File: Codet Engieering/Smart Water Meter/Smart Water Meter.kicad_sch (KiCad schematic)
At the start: 30 parts, among them J1 Barrel_Jack_Switch, J3 Conn_01x12_Pin, J4 Conn_01x07_Pin, J5 Conn_01x08_Pin, J6 Screw_Terminal_01x02, J6 Screw_Terminal_01x03, K2 SRD-05VDC-SL-C, Q2 BC547, U3 L7805CV

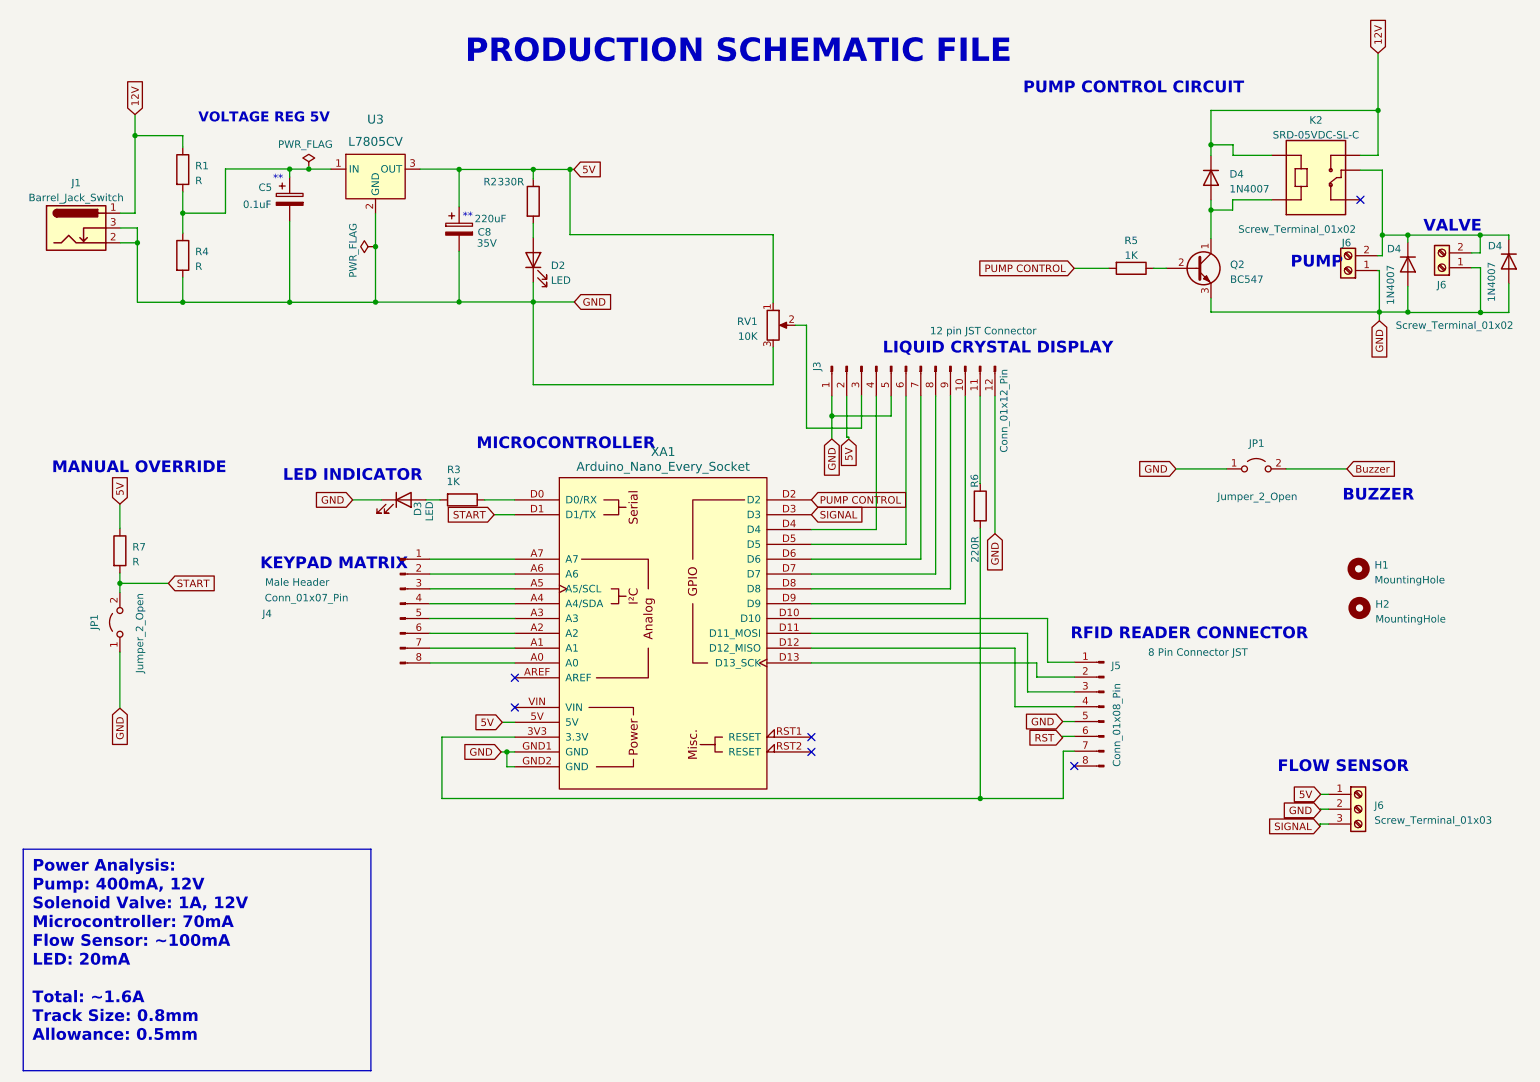
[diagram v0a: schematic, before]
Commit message: Redessigned the board to fit into asingle layer pcb for local production
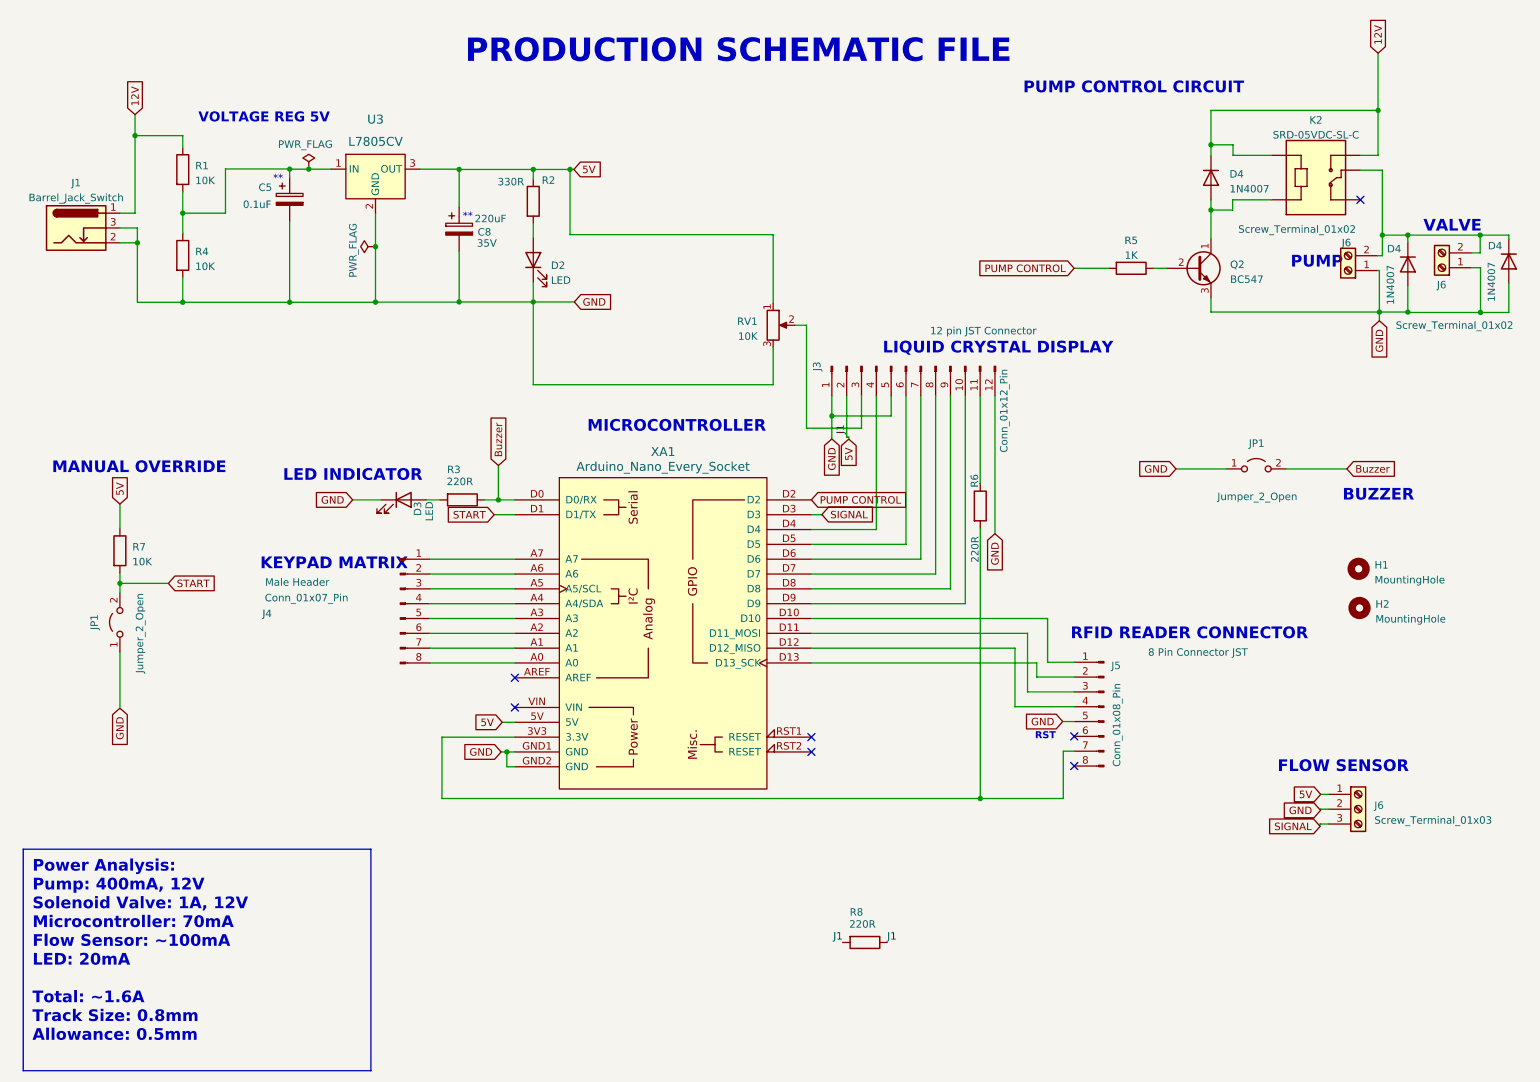
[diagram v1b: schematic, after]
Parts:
- added R8: 220R, Resistor_THT:R_Axial_DIN0207_L6.3mm_D2.5mm_P10.16mm_Horizontal, symbol Device:R
- R1, R4, R7: value R -> 10K
- R3: value 1K -> 220R
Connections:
- net 5V: now also R8.1, R8.2
- net Buzzer: now also R3.1, XA1.D0 (D0/RX)
- net RST: no longer names the net of J5.6 (Pin_6)
- no-connect marks 6 -> 7
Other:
- note added: "RST"
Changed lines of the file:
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@@
   (junction (at 107.3404 62.1538) (diameter 0) (color 0 0 0 0)
   )
+  (junction (at 101.3714 96.0628) (diameter 0) (color 0 0 0 0)
+  )
   (junction (at 68.8848 39.3954) (diameter 0) (color 0 0 0 0)
   )
@@
   (no_connect (at 200.025 141.6558))
   (no_connect (at 154.9908 136.7028))
+  (no_connect (at 200.025 136.5758))
   (wire (pts (xy 269.5702 53.7464) (xy 269.5702 50.6984))
     (stroke (width 0) (type default))
@@
     (stroke (width 0) (type default))
   )
-  (wire (pts (xy 99.0092 96.0628) (xy 104.1908 96.0628))
+  (wire (pts (xy 99.0092 96.0628) (xy 101.3714 96.0628))
     (stroke (width 0) (type default))
   )
@@
     (stroke (width 0) (type default))
   )
-  (wire (pts (xy 198.0184 136.5758) (xy 200.025 136.5758))
-    (stroke (width 0) (type default))
-  )
   (wire (pts (xy 104.1908 136.7028) (xy 91.694 136.7028))
     (stroke (width 0) (type default))
@@
     (stroke (width 0) (type default))
   )
+  (wire (pts (xy 101.3714 90.17) (xy 101.3714 96.0628))
+    (stroke (width 0) (type default))
+  )
   (wire (pts (xy 47.2948 62.2046) (xy 65.6082 62.2046))
     (stroke (width 0) (type default))
@@
     (stroke (width 0) (type default))
   )
+  (wire (pts (xy 156.7688 98.6028) (xy 154.9908 98.6028))
+    (stroke (width 0) (type default))
+  )
   (wire (pts (xy 195.453 116.3828) (xy 195.453 123.8758))
     (stroke (width 0) (type default))
@@
     (stroke (width 0) (type default))
   )
+  (wire (pts (xy 156.7942 98.5774) (xy 156.7688 98.5774))
+    (stroke (width 0) (type default))
+  )
   (wire (pts (xy 252.8062 54.229) (xy 252.0188 54.229))
     (stroke (width 0) (type default))
@@
     (stroke (width 0) (type default))
   )
-  (wire (pts (xy 198.0184 136.8044) (xy 198.0184 136.5758))
-    (stroke (width 0) (type default))
-  )
   (wire (pts (xy 198.1454 139.1158) (xy 200.025 139.1158))
     (stroke (width 0) (type default))
@@
     (stroke (width 0) (type default))
   )
+  (wire (pts (xy 101.3714 96.0628) (xy 104.1908 96.0628))
+    (stroke (width 0) (type default))
+  )
   (wire (pts (xy 94.6404 62.1538) (xy 107.3404 62.1538))
     (stroke (width 0) (type default))
@@
     (stroke (width 0) (type default))
   )
+  (wire (pts (xy 156.7688 98.5774) (xy 156.7688 98.6028))
+    (stroke (width 0) (type default))
+  )
   (wire (pts (xy 183.896 93.2942) (xy 183.9214 93.2942))
     (stroke (width 0) (type default))
@@
     (effects (font (size 4 4) (thickness 0.34) bold) (justify left bottom))
   )
+  (text "RST" (at 193.294 137.287 0)
+    (effects (font (size 1.2 1.2) bold) (justify left bottom))
+  )
   (text "BUZZER\n\n" (at 245.9736 99.7204 0)
     (effects (font (size 2 2) bold) (justify left bottom))
@@
     (effects (font (size 1.7 1.7) (thickness 0.34) bold) (justify left bottom))
   )
-  (text "MICROCONTROLLER" (at 97.6122 87.6808 0)
+  (text "MICROCONTROLLER" (at 116.586 84.709 0)
     (effects (font (size 2 2) bold) (justify left bottom))
   )
@@
     (effects (font (size 2 2) bold) (justify left bottom))
   )
+  (label "J1" (at 167.9702 171.8818 0) (fields_autoplaced)
+    (effects (font (size 1.27 1.27)) (justify left bottom))
+  )
+  (label "J1" (at 161.036 84.7598 90) (fields_autoplaced)
+    (effects (font (size 1.27 1.27)) (justify left bottom))
+  )
+  (label "J1" (at 160.3502 171.8818 180) (fields_autoplaced)
+    (effects (font (size 1.27 1.27)) (justify right bottom))
+  )
   (global_label "SIGNAL" (shape input) (at 242.1382 151.9936 180) (fields_autoplaced)
     (effects (font (size 1.27 1.27)) (justify right))
@@
     )
   )
+  (global_label "Buzzer" (shape input) (at 101.3714 90.17 90) (fields_autoplaced)
+    (effects (font (size 1.27 1.27)) (justify left))
+    (property "Intersheetrefs" "${INTERSHEET_REFS}" (at 101.3714 80.9142 90)
+      (effects (font (size 1.27 1.27)) (justify left) hide)
+    )
+  )
   (global_label "GND" (shape input) (at 242.2144 149.2504 180) (fields_autoplaced)
     (effects (font (size 1.27 1.27)) (justify right))
@@
     )
   )
-  (global_label "RST" (shape input) (at 198.0184 136.8044 180) (fields_autoplaced)
-    (effects (font (size 1.27 1.27)) (justify right))
-    (property "Intersheetrefs" "${INTERSHEET_REFS}" (at 191.6655 136.8044 0)
-      (effects (font (size 1.27 1.27)) (justify right) hide)
-    )
-  )
   (global_label "GND" (shape input) (at 114.3762 62.1538 0) (fields_autoplaced)
     (effects (font (size 1.27 1.27)) (justify left))
@@
     )
   )
-  (global_label "SIGNAL" (shape input) (at 154.9908 98.6028 0) (fields_autoplaced)
+  (global_label "SIGNAL" (shape input) (at 156.7942 98.5774 0) (fields_autoplaced)
     (effects (font (size 1.27 1.27)) (justify left))
-    (property "Intersheetrefs" "${INTERSHEET_REFS}" (at 164.4281 98.6028 0)
+    (property "Intersheetrefs" "${INTERSHEET_REFS}" (at 166.2315 98.5774 0)
       (effects (font (size 1.27 1.27)) (justify left) hide)
     )
@@
       (effects (font (size 1.27 1.27)) (justify left))
     )
-    (property "Value" "R" (at 49.4284 41.3766 0)
+    (property "Value" "10K" (at 49.4284 41.3766 0)
       (effects (font (size 1.27 1.27)) (justify left))
     )
@@
       (effects (font (size 1.27 1.27)) hide)
     )
+    (property "Details" "" (at 47.2948 39.4716 0)
+      (effects (font (size 1.27 1.27)))
+    )
     (pin "1")
     (pin "2")
@@
     )
   )
+  (symbol (lib_id "Device:R") (at 164.1602 171.8818 270) (unit 1)
+    (in_bom yes) (on_board yes) (dnp no)
+    (property "Reference" "R8" (at 161.544 166.7002 90)
+      (effects (font (size 1.27 1.27)) (justify left))
+    )
+    (property "Value" "220R" (at 161.4678 168.7576 90)
+      (effects (font (size 1.27 1.27)) (justify left))
+    )
+    (property "Footprint" "Resistor_THT:R_Axial_DIN0207_L6.3mm_D2.5mm_P10.16mm_Horizontal" (at 164.1602 170.1038 90)
+      (effects (font (size 1.27 1.27)) hide)
+    )
+    (property "Datasheet" "~" (at 164.1602 171.8818 0)
+      (effects (font (size 1.27 1.27)) hide)
+    )
+    (property "Details" "" (at 164.1602 171.8818 0)
+      (effects (font (size 1.27 1.27)))
+    )
+    (pin "1")
+    (pin "2")
+    (instances
+      (project "Smart Water Meter"
+        (path "/fc3c3691-f923-43ad-beea-061f9e930f37"
+          (reference "R8") (unit 1)
+        )
+      )
+    )
+  )
   (symbol (lib_id "power:PWR_FLAG") (at 68.8848 39.3954 0) (unit 1)
     (in_bom yes) (on_board yes) (dnp no)
@@
   (symbol (lib_id "Device:R") (at 107.3404 44.9072 0) (unit 1)
     (in_bom yes) (on_board yes) (dnp no)
-    (property "Reference" "R2" (at 98.806 41.5798 0)
+    (property "Reference" "R2" (at 108.7882 41.3258 0)
       (effects (font (size 1.27 1.27)) (justify left))
     )
@@
       (effects (font (size 1.27 1.27)) (justify left))
     )
-    (property "Value" "R" (at 49.4284 56.0832 0)
+    (property "Value" "10K" (at 49.4284 56.0832 0)
       (effects (font (size 1.27 1.27)) (justify left))
     )
@@
       (effects (font (size 1.27 1.27)) hide)
     )
+    (property "Details" "" (at 47.2948 54.1782 0)
+      (effects (font (size 1.27 1.27)))
+    )
     (pin "1")
     (pin "2")
@@
       (effects (font (size 1.27 1.27)) (justify left))
     )
-    (property "Value" "R" (at 38.6588 106.68 0)
+    (property "Value" "10K" (at 38.6588 106.68 0)
       (effects (font (size 1.27 1.27)) (justify left))
     )
@@
       (effects (font (size 1.27 1.27)) hide)
     )
+    (property "Details" "" (at 36.5252 104.775 0)
+      (effects (font (size 1.27 1.27)))
+    )
     (pin "1")
     (pin "2")
@@
       (effects (font (size 1.27 1.27)) (justify left))
     )
-    (property "Value" "1K" (at 92.5068 92.9386 90)
+    (property "Value" "220R" (at 92.5068 92.9386 90)
       (effects (font (size 1.27 1.27)) (justify left))
     )
